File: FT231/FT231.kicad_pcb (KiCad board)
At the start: 2 copper layers, 20.3 x 15.5 mm, 21 parts, among them J1 USB_B_Micro, J2 Conn_01x03, J3 Conn_01x03, J4 Conn_01x06, U1 FT231XQ

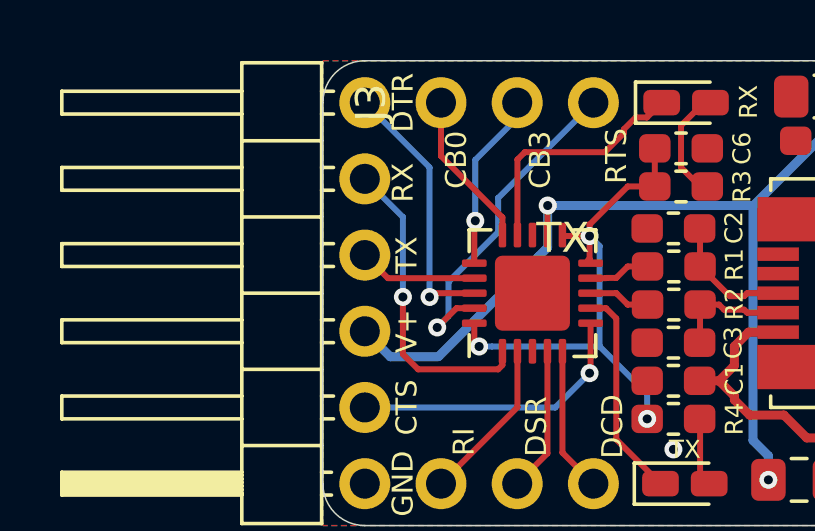
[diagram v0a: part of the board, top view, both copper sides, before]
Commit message: Silkscreens Updated
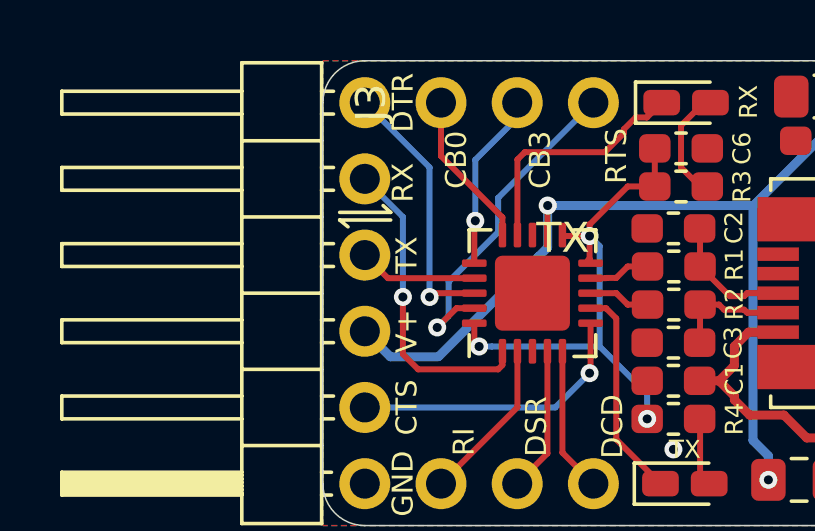
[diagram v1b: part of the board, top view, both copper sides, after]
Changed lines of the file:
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@@
   (general
     (thickness 1.6)
-    (drawings 31)
+    (drawings 35)
     (tracks 150)
     (zones 0)
@@
     (34 B.Paste user hide)
     (35 F.Paste user hide)
-    (36 B.SilkS user hide)
+    (36 B.SilkS user)
     (37 F.SilkS user)
     (38 B.Mask user hide)
@@
   )
   (setup
-    (last_trace_width 0.2)
+    (last_trace_width 0.127)
     (user_trace_width 0.15)
     (user_trace_width 0.2)
@@
     )
   )
+  (gr_line (start 192.2018 64.8716) (end 192.4812 65.1002) (layer F.SilkS) (width 0.12))
+  (gr_line (start 193.9036 64.8716) (end 192.2018 64.8716) (layer F.SilkS) (width 0.12))
+  (gr_line (start 193.9036 64.6176) (end 193.6496 64.389) (layer F.SilkS) (width 0.12))
+  (gr_line (start 192.2018 64.6176) (end 193.9036 64.6176) (layer F.SilkS) (width 0.12))
   (gr_text RTS (at 201.422 62.738 90) (layer F.SilkS)
     (effects (font (size 0.7 0.7) (thickness 0.15)))

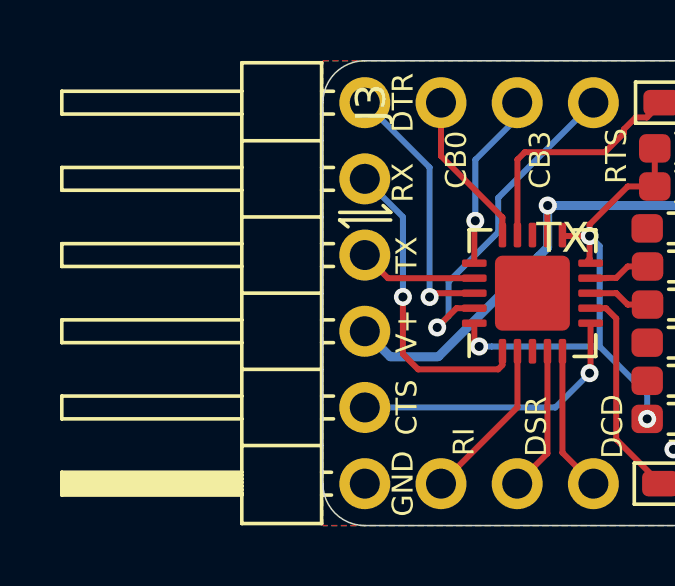
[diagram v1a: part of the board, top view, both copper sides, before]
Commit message: Silkscreen Updates
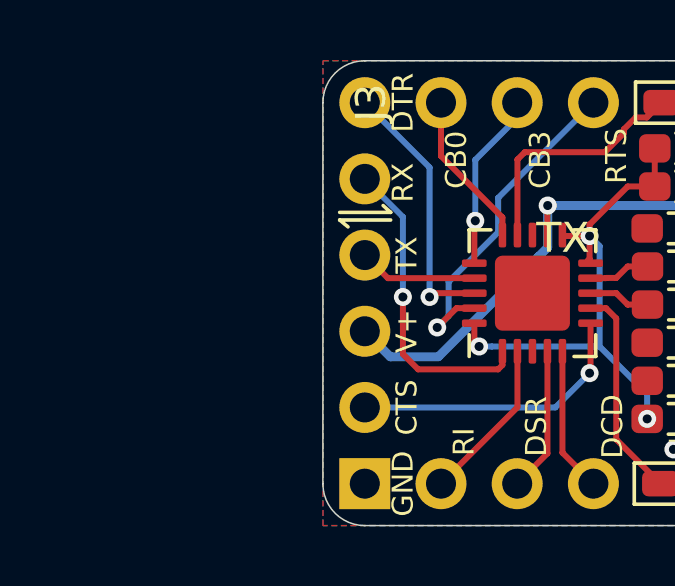
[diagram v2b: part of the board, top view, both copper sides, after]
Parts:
- J4: footprint Connector_PinHeader_2.54mm:PinHeader_1x06_P2.54mm_Horizontal -> Connector_PinHeader_2.54mm:PinHeader_1x06_P2.54mm_Vertical; moved to B.Cu
- turned J4 to 0 degrees
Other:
- board text added: "Full Handshake FT231X USB-UART"
- board text removed: "Full Handshake UART to USB"

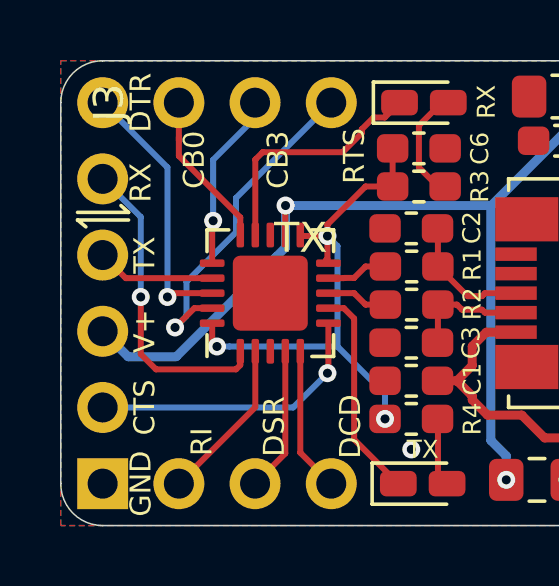
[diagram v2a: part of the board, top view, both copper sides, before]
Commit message: Dimensions Updated
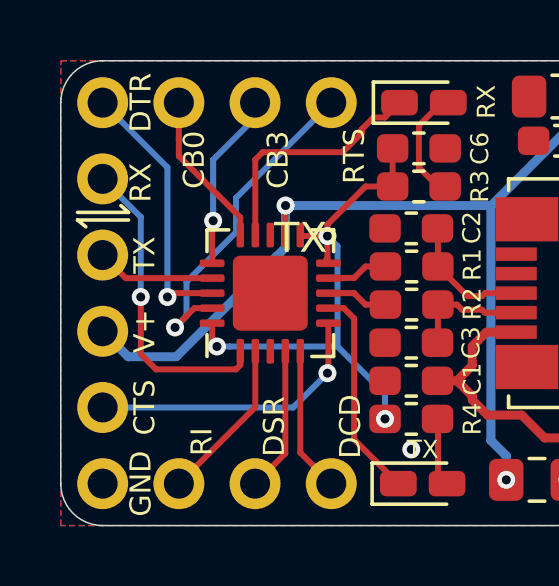
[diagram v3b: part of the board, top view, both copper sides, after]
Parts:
- J2, J3: moved to B.Cu
- J4: moved to F.Cu
- turned J2 to 270 degrees
- turned J3 to 270 degrees
- turned J4 to 180 degrees

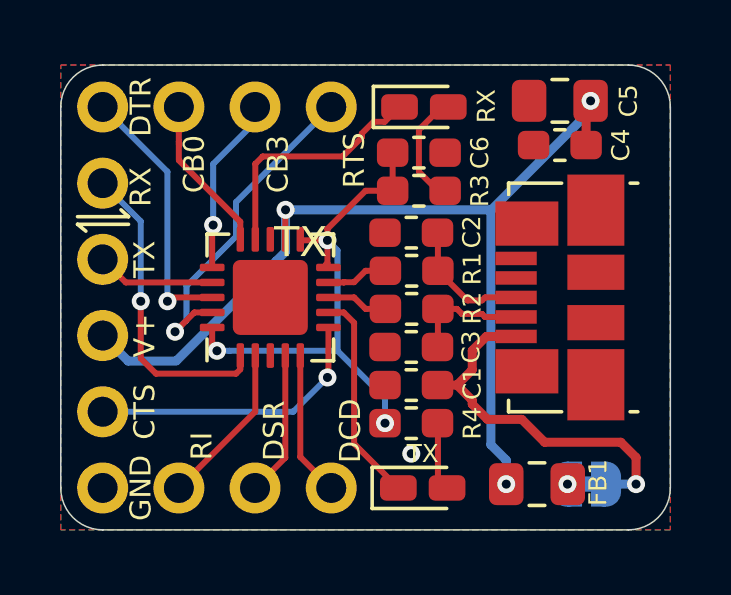
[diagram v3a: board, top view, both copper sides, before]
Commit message: Power LED Added
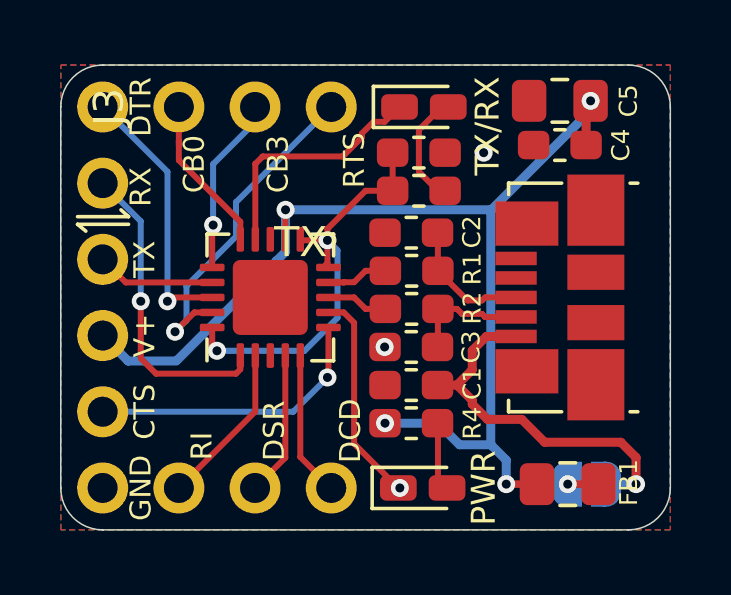
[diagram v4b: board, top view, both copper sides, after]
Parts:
- J2, J3: moved to F.Cu
- J4: moved to B.Cu
- JP1: footprint Jumper:SolderJumper-2_P1.3mm_Bridged_RoundedPad1.0x1.5mm -> Jumper:SolderJumper-2_P1.3mm_Open_RoundedPad1.0x1.5mm
- moved FB1 1.03 mm to (208.5, 73.5)
- turned J2 to 90 degrees
- turned J3 to 90 degrees
- turned J4 to 0 degrees
- renumbered TX to PWR, RX to TX/RX
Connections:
- net /RXLED renamed /TRX
- PWR pad 1: /TXLED -> GND
- R4 pad 1: Net-(C6-Pad1) -> /5V
- U1 pad 7: /TXLED -> Net-(U1-Pad7)
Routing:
- net /5V: track 33.1 -> 37.9 mm, vias 3 -> 4
- net Net-(C6-Pad1): track 18.0 -> 14.3 mm, vias 3 -> 2
- net Net-(FB1-Pad2): track 0.00 -> 1.03 mm
- net GND: vias 1 -> 3

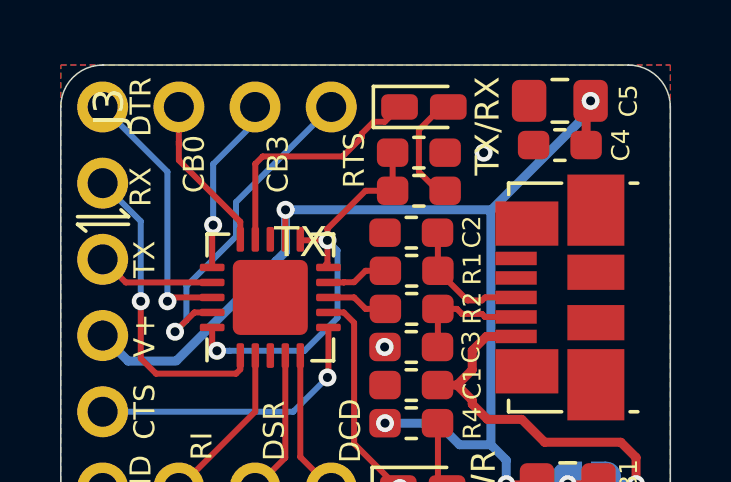
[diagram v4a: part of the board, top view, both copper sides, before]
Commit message: Power LED edited
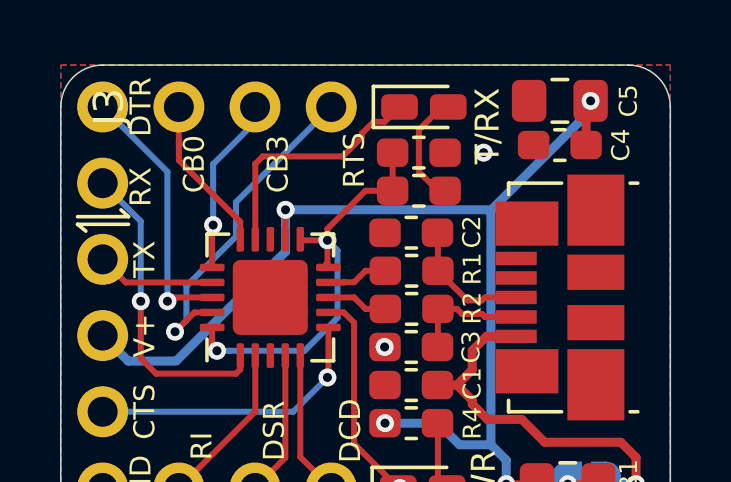
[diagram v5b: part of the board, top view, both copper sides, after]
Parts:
- R3, R4: value R_US -> 470E
- renumbered TX/RX to T/RX
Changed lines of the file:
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@@
   (general
     (thickness 1.6)
-    (drawings 37)
+    (drawings 36)
     (tracks 156)
     (zones 0)
@@
   )
   (setup
-    (last_trace_width 0.3)
+    (last_trace_width 0.127)
     (user_trace_width 0.15)
     (user_trace_width 0.2)
@@
       (effects (font (size 0.6 0.6) (thickness 0.12)))
     )
-    (fp_text value R_US (at 0 1.65) (layer F.Fab)
+    (fp_text value 470E (at 0 1.65) (layer F.Fab)
       (effects (font (size 1 1) (thickness 0.15)))
     )
@@
       (effects (font (size 0.6 0.6) (thickness 0.12)))
     )
-    (fp_text value R_US (at 0 1.65) (layer F.Fab)
+    (fp_text value 470E (at 0 1.65) (layer F.Fab)
       (effects (font (size 1 1) (thickness 0.15)))
     )
@@
     (tags "LED castellated")
     (attr smd)
-    (fp_text reference TX/RX (at 2.11836 0.635 270) (layer F.SilkS)
+    (fp_text reference T/RX (at 2.11836 0.635 270) (layer F.SilkS)
       (effects (font (size 0.8 0.8) (thickness 0.13)))
     )
@@
   (gr_text TX (at 194.437 66.04 90) (layer F.SilkS)
     (effects (font (size 0.7 0.7) (thickness 0.15)))
-  )
-  (gr_text TX (at 199.644 65.4685) (layer F.SilkS)
-    (effects (font (size 1 1) (thickness 0.15)))
   )
   (gr_text GND (at 194.31 73.66 90) (layer F.SilkS)
@@
   (segment (start 200.533 65.405) (end 200.868 65.74) (width 0.2) (layer B.Cu) (net 3))
   (segment (start 200.868 65.74) (end 200.868 67.991) (width 0.2) (layer B.Cu) (net 3))
-  (segment (start 204.56114 60.706) (end 204.343 60.706) (width 0.2) (layer F.Cu) (net 23))
-  (segment (start 204.216 63.754) (end 204.456 63.754) (width 0.2) (layer F.Cu) (net 23))
-  (segment (start 203.581 63.119) (end 204.216 63.754) (width 0.2) (layer F.Cu) (net 23))
-  (segment (start 203.581 61.722) (end 203.581 63.119) (width 0.2) (layer F.Cu) (net 23))
-  (segment (start 204.56114 60.96) (end 204.343 60.96) (width 0.2) (layer F.Cu) (net 23))
-  (segment (start 204.343 60.96) (end 203.581 61.722) (width 0.2) (layer F.Cu) (net 23))
   (segment (start 204.216 71.261) (end 204.202 71.247) (width 0.2) (layer F.Cu) (net 5))
   (segment (start 204.5205 73.66) (end 204.216 73.3555) (width 0.2) (layer F.Cu) (net 5))
@@
   (segment (start 199.39 71.12) (end 193.04 71.12) (width 0.2) (layer B.Cu) (net 21))
   (segment (start 200.533 69.977) (end 199.39 71.12) (width 0.2) (layer B.Cu) (net 21))
+  (segment (start 201.078 67.81) (end 201.422 68.154) (width 0.2) (layer F.Cu) (net 22))
+  (segment (start 200.5655 67.81) (end 201.078 67.81) (width 0.2) (layer F.Cu) (net 22))
+  (segment (start 201.422 72.1865) (end 202.8955 73.66) (width 0.2) (layer F.Cu) (net 22))
+  (segment (start 201.422 68.154) (end 201.422 72.1865) (width 0.2) (layer F.Cu) (net 22))
+  (segment (start 204.56114 60.706) (end 204.343 60.706) (width 0.2) (layer F.Cu) (net 23))
+  (segment (start 204.216 63.754) (end 204.456 63.754) (width 0.2) (layer F.Cu) (net 23))
+  (segment (start 203.581 63.119) (end 204.216 63.754) (width 0.2) (layer F.Cu) (net 23))
+  (segment (start 203.581 61.722) (end 203.581 63.119) (width 0.2) (layer F.Cu) (net 23))
+  (segment (start 204.56114 60.96) (end 204.343 60.96) (width 0.2) (layer F.Cu) (net 23))
+  (segment (start 204.343 60.96) (end 203.581 61.722) (width 0.2) (layer F.Cu) (net 23))
   (segment (start 202.81407 60.706) (end 202.93614 60.706) (width 0.2) (layer F.Cu) (net 24))
   (segment (start 198.128 62.857) (end 198.128 65.3725) (width 0.2) (layer F.Cu) (net 24))
@@
   (segment (start 201.676 61.849) (end 201.676 61.976) (width 0.2) (layer F.Cu) (net 24))
   (segment (start 201.041 62.611) (end 198.374 62.611) (width 0.2) (layer F.Cu) (net 24))
-  (segment (start 201.078 67.81) (end 201.422 68.154) (width 0.2) (layer F.Cu) (net 22))
-  (segment (start 200.5655 67.81) (end 201.078 67.81) (width 0.2) (layer F.Cu) (net 22))
-  (segment (start 201.422 72.1865) (end 202.8955 73.66) (width 0.2) (layer F.Cu) (net 22))
-  (segment (start 201.422 68.154) (end 201.422 72.1865) (width 0.2) (layer F.Cu) (net 22))
   (zone (net 1) (net_name GND) (layer F.Cu) (hatch none 0.508)
     (connect_pads (clearance 0.15))

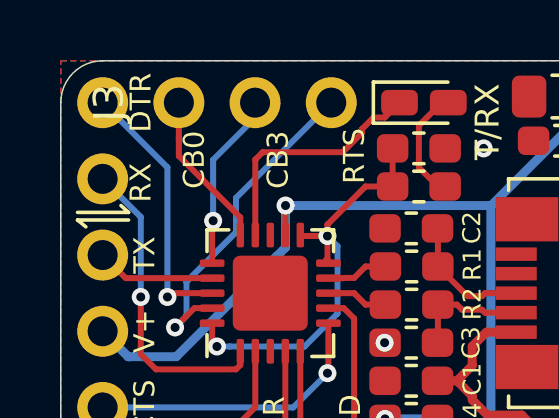
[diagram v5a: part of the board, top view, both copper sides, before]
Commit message: Silkscreen Edits
Dimensions moved to Drawings Layer
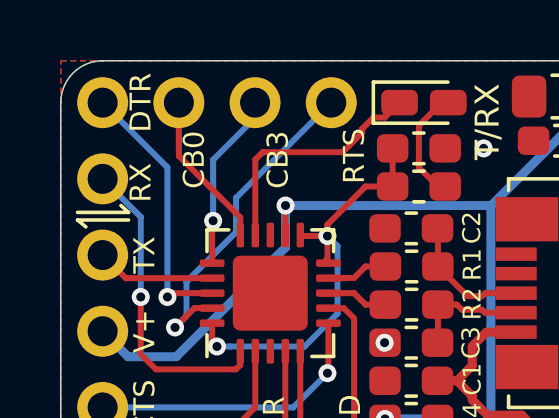
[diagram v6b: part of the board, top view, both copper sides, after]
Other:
- rule pad_to_mask_clearance: 0.051 -> 0
- rule solder_mask_min_width: 0.25 -> 0.1
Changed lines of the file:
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@@
     (pad_size 1.7 1.7)
     (pad_drill 1)
-    (pad_to_mask_clearance 0.051)
-    (solder_mask_min_width 0.25)
+    (pad_to_mask_clearance 0)
+    (solder_mask_min_width 0.1)
     (aux_axis_origin 0 0)
     (visible_elements 7FFFFFFF)
     (pcbplotparams
-      (layerselection 0x010fc_ffffffff)
+      (layerselection 0x010f0_ffffffff)
       (usegerberextensions false)
       (usegerberattributes false)
@@
       (viasonmask false)
       (mode 1)
-      (useauxorigin false)
+      (useauxorigin true)
       (hpglpennumber 1)
       (hpglpenspeed 20)
@@
       (psa4output false)
       (plotreference true)
-      (plotvalue true)
+      (plotvalue false)
       (plotinvisibletext false)
       (padsonsilk false)
@@
       (outputformat 1)
       (mirror false)
-      (drillshape 1)
+      (drillshape 0)
       (scaleselection 1)
-      (outputdirectory ""))
+      (outputdirectory "../../Gerbers/FT231X/"))
   )
   (net 0 "")
@@
     (descr "Through hole straight pin header, 1x03, 2.54mm pitch, single row")
     (tags "Through hole pin header THT 1x03 2.54mm single row")
-    (fp_text reference J3 (at 0 -2.33 90) (layer F.SilkS)
+    (fp_text reference J3 (at 0 -2.54 90) (layer F.SilkS) hide
       (effects (font (size 1 1) (thickness 0.15)))
     )
@@
     )
   )
-  (dimension 7.62 (width 0.12) (layer F.SilkS)
-    (gr_text "7.620 mm" (at 196.85 56.515) (layer F.SilkS)
+  (dimension 7.62 (width 0.12) (layer Dwgs.User)
+    (gr_text "7.620 mm" (at 196.85 56.515) (layer Dwgs.User)
       (effects (font (size 1 1) (thickness 0.15)) hide)
     )
@@
     (arrow2b (pts (xy 193.04 57.785) (xy 194.166504 57.198579)))
   )
-  (dimension 12.7 (width 0.12) (layer F.SilkS)
-    (gr_text "12.700 mm" (at 188.214 67.31 90) (layer F.SilkS)
+  (dimension 12.7 (width 0.12) (layer Dwgs.User)
+    (gr_text "12.700 mm" (at 188.214 67.31 90) (layer Dwgs.User)
       (effects (font (size 1 1) (thickness 0.15)) hide)
     )
@@
     (arrow2b (pts (xy 189.484 73.66) (xy 188.897579 72.533496)))
   )
-  (dimension 15.494 (width 0.12) (layer F.SilkS)
-    (gr_text "15.494 mm" (at 185.293 67.31 90) (layer F.SilkS)
+  (dimension 15.494 (width 0.12) (layer Dwgs.User)
+    (gr_text "15.494 mm" (at 185.293 67.31 90) (layer Dwgs.User)
       (effects (font (size 1 1) (thickness 0.15)))
     )
@@
     (effects (font (size 0.7 0.7) (thickness 0.15)))
   )
-  (dimension 20.32 (width 0.12) (layer F.SilkS)
-    (gr_text "20.320 mm" (at 201.803 53.848) (layer F.SilkS)
+  (dimension 20.32 (width 0.12) (layer Dwgs.User)
+    (gr_text "20.320 mm" (at 201.803 53.848) (layer Dwgs.User)
       (effects (font (size 1 1) (thickness 0.15)) hide)
     )

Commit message: Page Settings Updated
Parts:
- moved C1 135.4 mm to (70.1, 45.8)
- moved C2 135.4 mm to (70.1, 40.8)
- moved C3 135.4 mm to (70.1, 44.6)
- moved C4 135.4 mm to (75.1, 37.8)
- moved C5 135.4 mm to (75.1, 36.4)
- moved FB1 135.4 mm to (75.3, 49.1)
- moved G*** 135.4 mm to (65.5, 42.9)
- moved J1 135.4 mm to (75.1, 42.9)
- moved J2 135.4 mm to (62.4, 49.3)
- moved J3 135.4 mm to (62.4, 36.6)
- moved JP1 135.4 mm to (75.9, 49.1)
- moved PWR 135.4 mm to (70.5, 49.3)
- moved R1 135.4 mm to (70.1, 42.0)
- moved R2 135.4 mm to (70.1, 43.3)
- moved R4 135.4 mm to (70.1, 47.1)
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
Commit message: Part Numbers Added
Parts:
- removed the PWR at (70.5, 49.3)
- removed T/RX: RX, LED_SMD:LED_0603_1608Metric_Castellated
- added PWR: RED, LED_SMD:LED_0603_1608Metric, F.Cu at (76.6, 49.3)
- added R5: 680E, Resistor_SMD:R_0603_1608Metric, F.Cu at (70.4, 48.1)
- added RX: GREEN, LED_SMD:LED_0603_1608Metric, F.Cu at (70.4, 36.2)
- added TX: GREEN, LED_SMD:LED_0603_1608Metric, F.Cu at (70.4, 49.5)
- C1, C2, C3, C6: footprint Capacitor_SMD:C_0603_1608Metric_Pad1.05x0.95mm_HandSolder -> Capacitor_SMD:C_0603_1608Metric
- FB1: value Ferrite_Bead -> 40E@100MHz; footprint Inductor_SMD:L_0805_2012Metric_Pad1.15x1.40mm_HandSolder -> Inductor_SMD:L_0603_1608Metric
- JP1: value SolderJumper_2_Open -> SolderJumper_2_Bridged; footprint Jumper:SolderJumper-2_P1.3mm_Open_RoundedPad1.0x1.5mm -> Jumper:SolderJumper-2_P1.3mm_Bridged_RoundedPad1.0x1.5mm
- R1, R2: footprint Resistor_SMD:R_0603_1608Metric_Pad1.05x0.95mm_HandSolder -> Resistor_SMD:R_0603_1608Metric
- R3, R4: value 470E -> 680E; footprint Resistor_SMD:R_0603_1608Metric_Pad1.05x0.95mm_HandSolder -> Resistor_SMD:R_0603_1608Metric
- moved JP1 3.75 mm to (72.6, 47.4), turned to 270 degrees
- moved R3 1.78 mm to (70.4, 37.6)
- moved FB1 1.18 mm to (74.2, 48.9), turned to 90 degrees
- moved C6 0.76 mm to (70.4, 38.9)
- moved C2 0.57 mm to (70.4, 40.3)
- moved C3 0.57 mm to (70.4, 44.1)
- moved R2 0.56 mm to (70.4, 42.8)
- moved R1 0.56 mm to (70.4, 41.5)
- moved C1 0.46 mm to (70.4, 45.5)
- moved R4 0.46 mm to (70.4, 46.7)
- moved J4 0.38 mm to (59.4, 49.3)
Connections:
- U1 pad 14: /TRX -> /RXLED
- U1 pad 7: Net-(U1-Pad7) -> /TXLED
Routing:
- net /TRX: track 8.31 -> 0.00 mm
- net /RXLED: track 0.00 -> 8.12 mm
- net Net-(C1-Pad1): track 12.6 -> 4.94 mm
- net Net-(C6-Pad1): track 14.3 -> 20.6 mm, vias 2 -> 3
- net Net-(PWR1-Pad2): track 2.54 -> 6.31 mm
- net Net-(R3-Pad2): track 4.05 -> 1.40 mm
- net GND: track 0.00 -> 2.49 mm, vias 3 -> 0
- net /5V: track 37.9 -> 40.2 mm
- net Net-(FB1-Pad2): track 1.03 -> 2.87 mm
- net Net-(R5-Pad2): track 0.00 -> 1.40 mm
- net /TXLED: track 7.12 -> 7.85 mm
- net /uD+: track 2.06 -> 2.60 mm
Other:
- board size 20.3 x 15.5 mm -> 20.7 x 15.5 mm
